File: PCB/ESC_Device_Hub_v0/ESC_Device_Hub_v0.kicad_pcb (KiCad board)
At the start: 2 copper layers, 50 x 90 mm, 141 parts, among them J1 Conn_01x04, J10 Conn_01x06, J11 Conn_01x02, J12 Conn_01x02, J13 Conn_01x02, J14 Conn_01x02, J15 Conn_01x02, J16 Conn_01x02, J17 Conn_01x02, J18 Conn_01x02, J19 Conn_01x05, J2 Conn_01x04, J20 Conn_01x01, J21 Conn_01x01, J22 Conn_01x02, J3 Conn_01x04, J4 Conn_01x04, J5 Conn_01x04, J6 Conn_01x04, J7 Conn_01x06, J8 Conn_01x06, J9 Conn_01x06, SW1 SW_Push, SW2 SW_Push, SW3 SW_Coded_SH-7050, SW4 SW_DIP_x02, U1 ISO1042BQDWVQ1, U18 USB_Type-C, U2 MCP2562FD-H/MF, U3 IS25LP064D-JLLE, U4 STM32H563RGVx, U5 NJW1933F1-AT, U6 TLP293, U7 NJM2884U1-33, U8 XC8114AA01PR-G, U9 XC8114AA01PR-G, Y1 FC2012SN 32.768K-70NNA0KC0

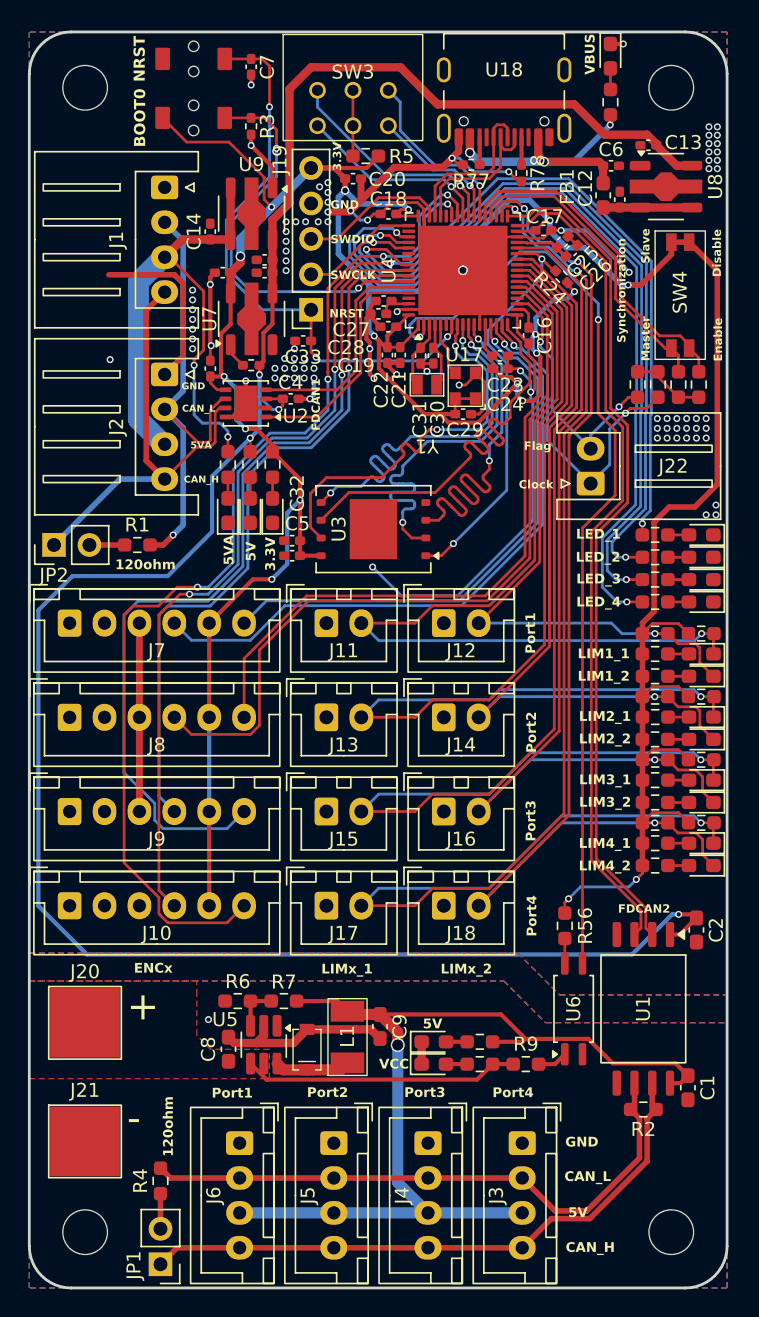
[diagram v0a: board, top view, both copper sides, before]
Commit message: CANFDのXHを縦にして発振器を変更
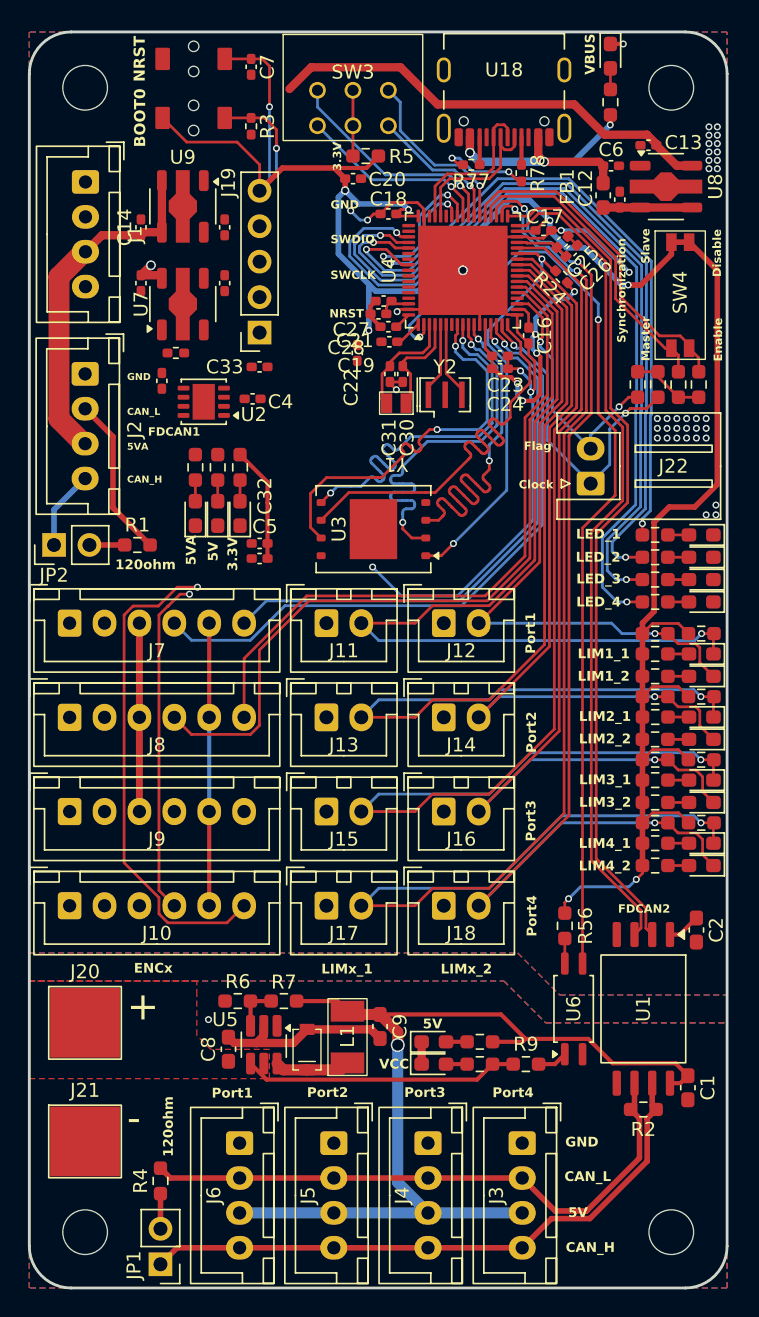
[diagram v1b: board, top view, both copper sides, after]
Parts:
- removed C29: 0.1uF, Capacitor_SMD:C_0402_1005Metric_Pad0.74x0.62mm_HandSolder
- removed U17: ~, My_Library:ECS-TXO-2520-33-500-AN-TR
- added Y2: Crystal_GND2, Crystal:Resonator_SMD_Murata_CSTxExxV-3Pin_3.0x1.1mm, F.Cu at (169.8, 56.0)
- J1, J2: footprint Connector_JST:JST_XH_S4B-XH-A_1x04_P2.50mm_Horizontal -> Connector_JST:JST_XH_B4B-XH-A_1x04_P2.50mm_Vertical
- moved C10 5.91 mm to (148.0, 48.0), turned to -90 degrees
- moved J2 5.70 mm to (144.0, 54.5)
- moved J1 5.69 mm to (144.0, 40.8)
- moved R18 5.47 mm to (150.5, 53.0)
- moved U7 5.04 mm to (151.0, 49.5)
- moved C14 4.98 mm to (148.0, 44.0)
- moved U9 4.95 mm to (151.0, 42.5)
- moved J19 4.03 mm to (156.5, 51.5)
- moved C15 3.69 mm to (154.0, 44.0), turned to 90 degrees
- moved C33 3.63 mm to (156.5, 54.0)
- moved C3 3.58 mm to (149.5, 55.0)
- moved U2 3.01 mm to (152.5, 56.5)
- moved C11 2.96 mm to (154.0, 48.0), turned to -90 degrees
- moved C4 2.73 mm to (156.0, 56.3)
- moved C30 2.56 mm to (166.8, 54.5)
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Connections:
- U4 pad 5: OSC -> Net-(U4-PH0)
- U4 pad 6: unconnected-(U4-PH1-Pad6) -> Net-(U4-PH1)
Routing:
- net +5V: track 159.5 -> 34.8 mm, vias 4 -> 0
- net ENC3_A: track 62.4 -> 0.00 mm, vias 1 -> 0
- net +3.3V: track 260.9 -> 201.7 mm, vias 18 -> 13
- net GND: track 165.6 -> 107.5 mm, vias 93 -> 46
- net ENC3_B: track 51.5 -> 0.00 mm, vias 1 -> 0
- net ENC4_B: track 65.4 -> 32.2 mm, vias 4 -> 3
- net ENC4_A: track 77.1 -> 44.9 mm, vias 4 -> 3
- net NRST: track 41.5 -> 11.4 mm, vias 3 -> 1
- net CAN_H: track 32.1 -> 5.68 mm
- net CAN_L: track 34.2 -> 11.7 mm, vias 1 -> 0
- net BOOT0: track 29.2 -> 7.43 mm, vias 2 -> 1
- net FDCAN_TXD: track 16.9 -> 0.00 mm
- net +5VA: track 41.4 -> 25.2 mm, vias 2 -> 0
- net FDCAN_RXD: track 16.2 -> 0.00 mm
- net SWDIO: track 10.6 -> 0.00 mm
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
